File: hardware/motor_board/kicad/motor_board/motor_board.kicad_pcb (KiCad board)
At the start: 6 copper layers, 75 x 35 mm, 237 parts, among them J1 BOOMELE_1.27-2x10P, J2 WAFER-SH1.0-6PWB, J3 WAFER-SH1.0-6PWB, J4 S5B-XH-A, Q1 HYG015N04LS1C2, Q2 HYG015N04LS1C2, Q3 HYG015N04LS1C2, Q4 HYG015N04LS1C2, Q5 HYG015N04LS1C2, Q6 HYG015N04LS1C2, Q7 HYG015N04LS1C2, Q8 HYG015N04LS1C2, U1 STM32G474RET6, U10 SN74LVC3G17DCUR, U11 TPS22945DCKR, U12 TPS22945DCKR, U13 LM74502DDFR, U14 74LVC1G17SE-7, U2 DRV8323RHRGZR, U3 DRV8316CRRGFR, U4 DRV8316CRRGFR, U5 AP2112K-3.3TRG1, U6 SN74LVC08APWR, U7 INA239AIDGSR, U8 BQ76907RGRR, U9 SN74LVC3G17DCUR

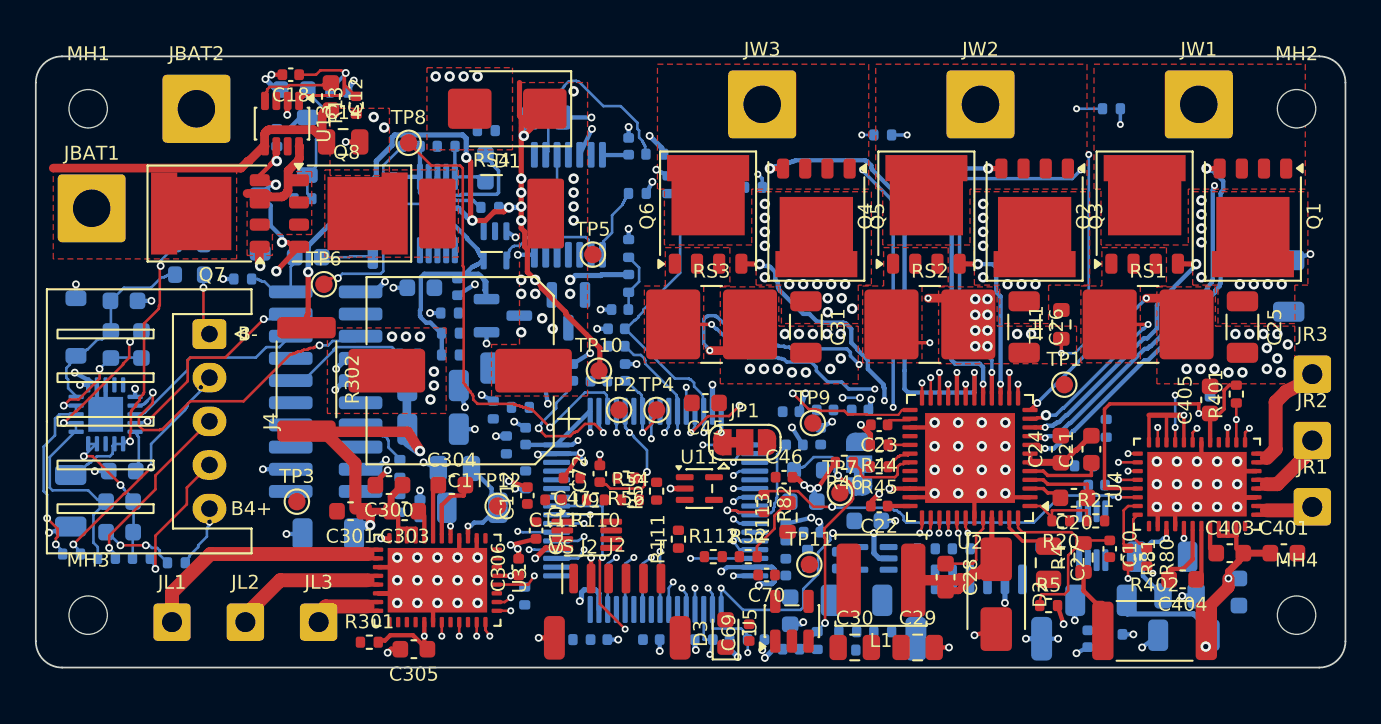
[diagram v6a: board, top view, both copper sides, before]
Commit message: motor_board routing 12a/12b0/12b: U2 west escapes, U6 escape, U2 rear bus on L4, hub nets on L4
U2 pins 28/33 escape west between the mode resistors (redundant pin-34 GND via dropped);
U6's signal pins escape between its rows / into the VBAT via row gap (RS4's VBAT pad is
over U6's middle; D7 nudged 0.6 mm; R63 takes its own VBAT via); U1 pins 8/9 out north;
the six U2 rear lines fanned out by hand into lane order INLC/INLB/INLA | INHA | INHB/INHC
and routed inside-out on L4 (17-28 mm, INLC 41 mm). DRC 0, 235 unconnected.

Co-Authored-By: Claude Opus 5.5 (1M context) <noreply@anthropic.com>
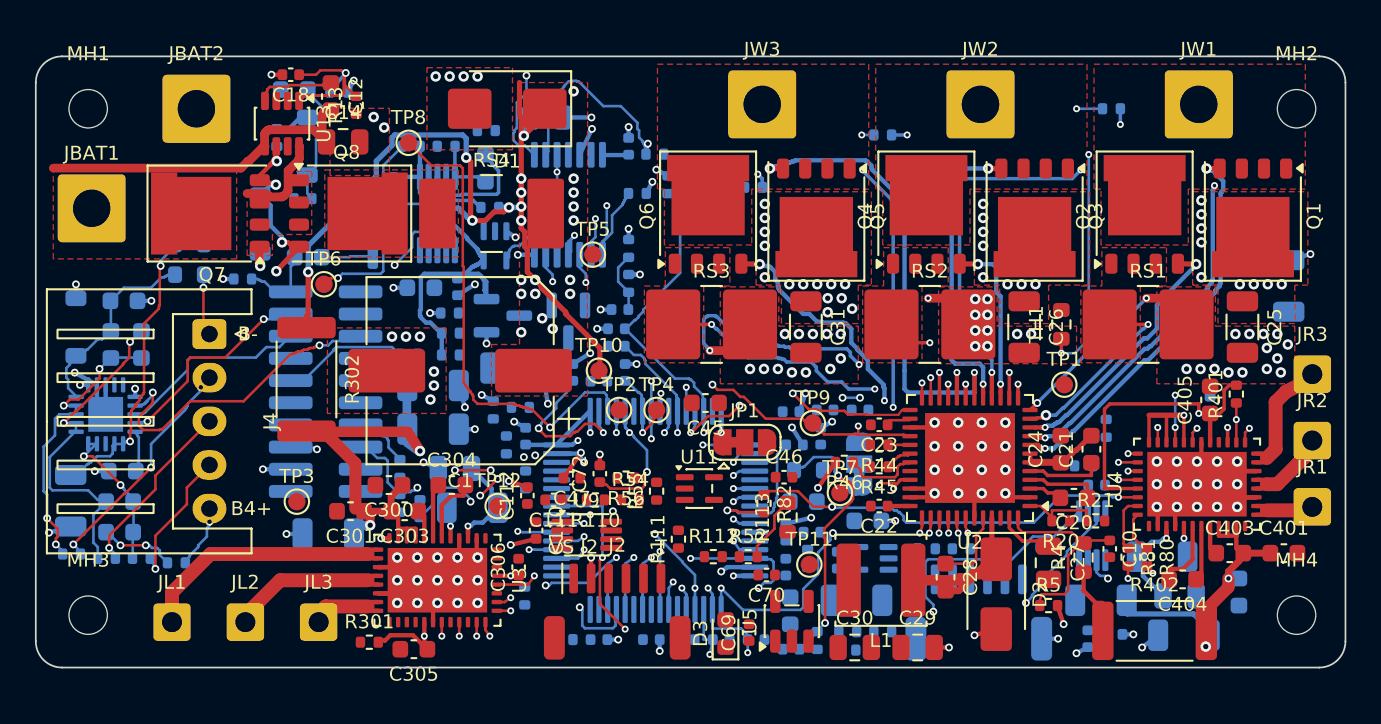
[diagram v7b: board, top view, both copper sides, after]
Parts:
- moved D7 0.60 mm to (130.5, 85.2)
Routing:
- net W_INLC_M: track 13.0 -> 58.9 mm, vias 1 -> 3
- net /weapon/W_INLC: track 0.72 -> 45.1 mm, vias 1 -> 2
- net GND: track 119.9 -> 75.9 mm, vias 190 -> 153
- net R_S2: track 1.93 -> 39.8 mm, vias 1 -> 2
- net R_S1: track 1.84 -> 35.7 mm, vias 1 -> 2
- net INA_nCS: track 9.44 -> 43.2 mm, vias 0 -> 2
- net /weapon/W_INLB: track 0.70 -> 32.8 mm, vias 1 -> 2
- net W_INLB_M: track 1.22 -> 31.9 mm, vias 1 -> 5
- net /weapon/W_INLA: track 0.71 -> 28.4 mm, vias 1 -> 2
- net /mcu/MB_TX: track 1.23 -> 27.6 mm, vias 1 -> 4
- net R_S3: track 3.68 -> 28.6 mm, vias 1 -> 3
- net /mcu/MB_RX: track 1.31 -> 26.1 mm, vias 1 -> 4
- net W_nFAULT: track 10.6 -> 32.1 mm, vias 2 -> 4
- net W_INHB: track 0.70 -> 22.2 mm, vias 1 -> 2
- net W_INHA: track 2.30 -> 23.0 mm, vias 2 -> 3
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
